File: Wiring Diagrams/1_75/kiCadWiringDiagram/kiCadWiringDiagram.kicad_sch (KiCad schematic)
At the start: 0 parts

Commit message: Designing schematic
Completed dual 12V inputs and converting them to 5V.

The rest of the circuit still remains.
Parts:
- added C1: C_Small, symbol Device:C_Small
- added C2, C3: C_Polarized_Small, symbol Device:C_Polarized_Small
- added D1, D2, D3: D_Schottky, symbol Device:D_Schottky
- added F1, F2: Fuse, symbol Device:Fuse
- added J1: ESP32, symbol Connector:Conn_01x10_Socket
- added J10: Boost Converter Input, symbol Connector:Conn_01x02_Socket
- added J11: Magnetometer MMC5603, symbol Connector:Conn_01x04_Socket
- added J12: Speaker Connector, symbol Connector:Conn_01x02_Socket
- added J2: Encoder Connector, symbol Connector:Conn_01x03_Socket
- added J3: LED Connector, symbol Connector:Conn_01x03_Socket
- added J4: Motor Connector, symbol Connector:Conn_01x03_Socket
- added J5: 12v Input 1, symbol Connector:Conn_01x02_Socket
- added J6: 12v Input 2, symbol Connector:Conn_01x02_Socket
- added J9: Boost Converter Output, symbol Connector:Conn_01x02_Socket
- added L1: L_Small, symbol Device:L_Small
- added U1: LM2596S-5, Package_TO_SOT_SMD:TO-263-5_TabPin3, symbol Regulator_Switching:LM2596S-5
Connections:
- new net: C3.1, L1.1, U1.4 (FB)
- new net: D3.2 (A), J5.1 (Pin_1), J6.1 (Pin_1), U1.3 (GND), U1.5 (~{ON}/OFF)
- new net: F1.2, J6.2 (Pin_2)
- new net: C1.1, C2.1, D1.1 (K), D2.1 (K)
- new net: D1.2 (A), F1.1
- new net: C1.2, C2.2, U1.1 (VIN)
- new net: D3.1 (K), L1.2, U1.2 (OUT)
- new net: D2.2 (A), F2.1
- new net: F2.2, J5.2 (Pin_2)

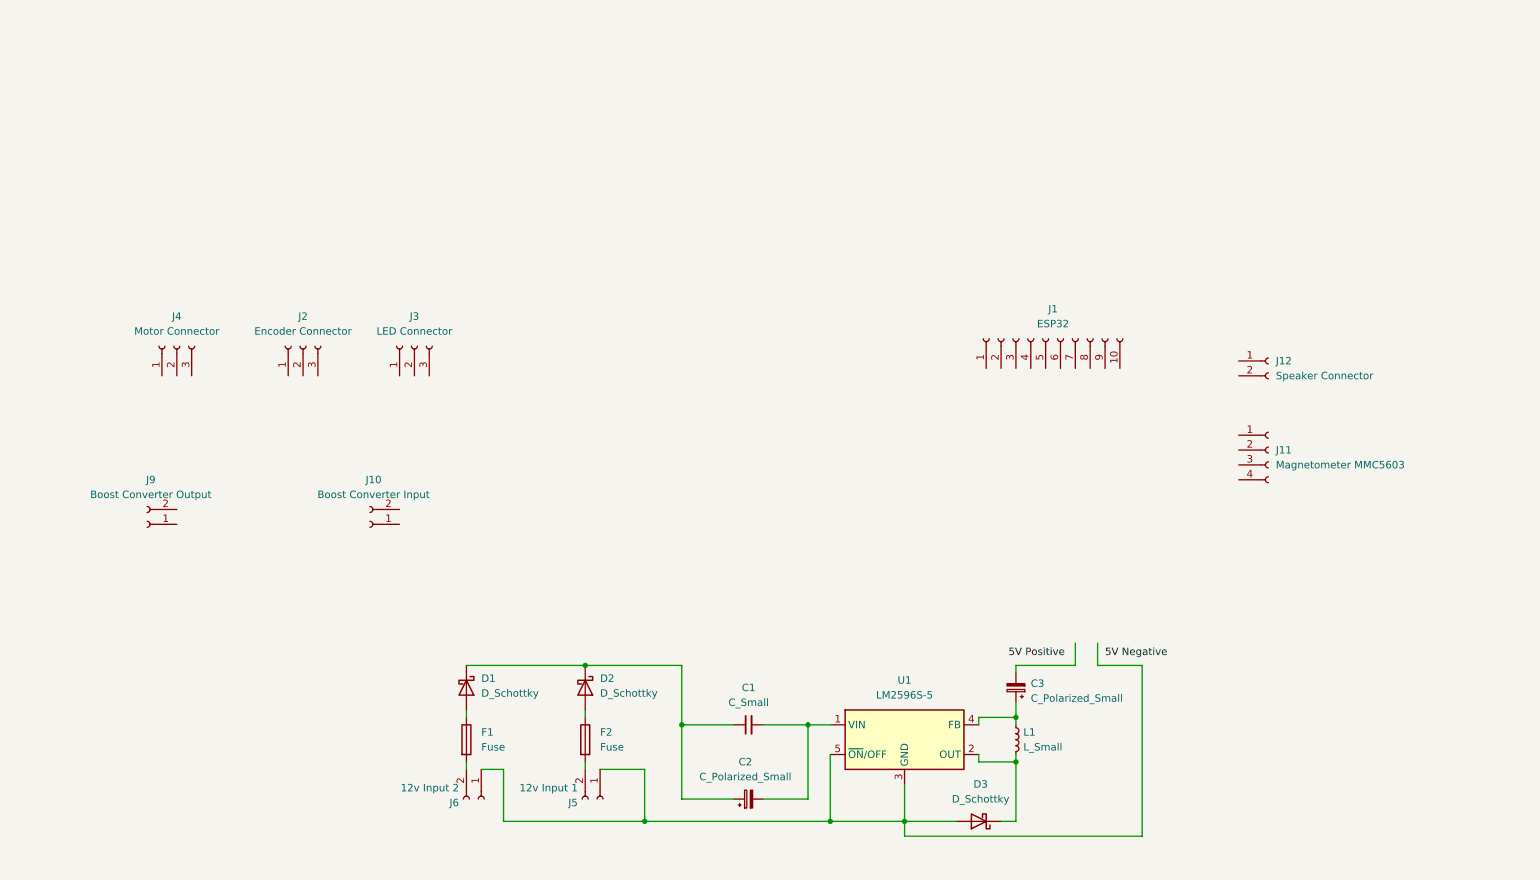
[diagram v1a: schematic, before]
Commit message: 5v to 10v conversion looks complete
fixed polarized capacitors
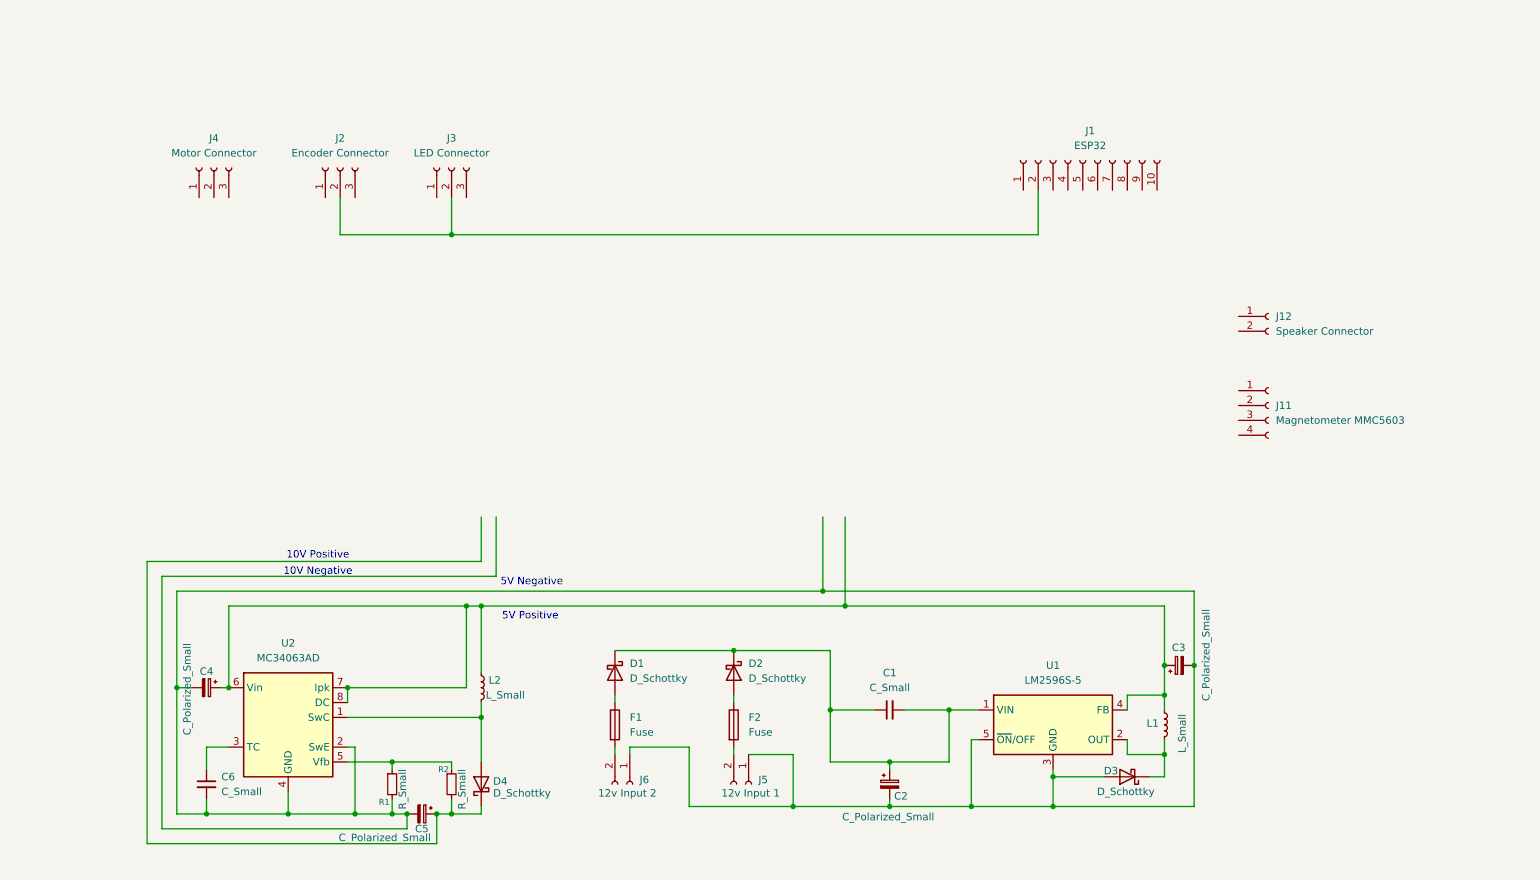
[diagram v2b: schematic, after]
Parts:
- removed J10: Boost Converter Input, symbol Connector:Conn_01x02_Socket
- removed J9: Boost Converter Output, symbol Connector:Conn_01x02_Socket
- added C4, C5: C_Polarized_Small, symbol Device:C_Polarized_Small
- added C6: C_Small, symbol Device:C_Small
- added D4: D_Schottky, symbol Device:D_Schottky
- added L2: L_Small, symbol Device:L_Small
- added R1, R2: R_Small, symbol Device:R_Small
- added U2: MC34063AD, Package_SO:SOIC-8_3.9x4.9mm_P1.27mm, symbol Regulator_Switching:MC34063AD
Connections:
- net at J1.2 (Pin_2): now also J2.2 (Pin_2), J3.2 (Pin_2)
- net at C3.1, L1.1, U1.4 (FB): now also C4.1, L2.1, U2.6 (Vin), U2.7 (Ipk), U2.8 (DC)
- net at C3.2: now also C2.2, D3.2 (A), J5.1 (Pin_1), J6.1 (Pin_1), U1.3 (GND), U1.5 (~{ON}/OFF), C4.2, C5.2, C6.2, R1.2, U2.2 (SwE), U2.4 (GND)
- net at C1.1, C2.1, D1.1 (K)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: now also C1.2, U1.1 (VIN)
- new net: D4.2 (A), L2.2, U2.1 (SwC)
- new net: C6.1, U2.3 (TC)
- new net: R1.1, R2.1, U2.5 (Vfb)
- new net: C5.1, D4.1 (K), R2.2
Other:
- note added: "10V Negative"
- note added: "10V Positive"
- note added: "5V Negative"
- note added: "5V Positive"
- moved on the sheet: C1, C2, C3, D1, D2, D3, F1, F2, J1, J11, J12, J2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

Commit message: Schematic done I think
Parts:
- removed J11: Magnetometer MMC5603, symbol Connector:Conn_01x04_Socket
- added U3: MMC5603NJ, MMC5603NJ:XDCR_MMC5603NJ, symbol MMC5603NJ:MMC5603NJ
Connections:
- net at J4.1 (Pin_1): now also C5.1, D4.1 (K), R2.2
- net at J4.2 (Pin_2): now also C2.2, C3.2, C4.2, C5.2, C6.2, D3.2 (A), J1.1 (Pin_1), J1.2 (Pin_2), J2.2 (Pin_2), J3.1 (Pin_1), J3.2 (Pin_2), J5.1 (Pin_1), J6.1 (Pin_1), R1.2, U1.3 (GND), U1.5 (~{ON}/OFF), U2.2 (SwE), U2.4 (GND), U3.A1 (VSA)
- net at J4.3 (Pin_3): now also J1.6 (Pin_6)
- net at J1.10 (Pin_10): now also J12.1 (Pin_1)
- net at J1.3 (Pin_3): now also J2.1 (Pin_1), U3.B1 (VDD)
- net at J1.4 (Pin_4): now also J3.3 (Pin_3)
- net at J1.5 (Pin_5): now also J2.3 (Pin_3)
- net at J1.7 (Pin_7): now also U3.B2 (SDA)
- net at J1.8 (Pin_8): now also U3.A2 (SCL)
- net at J1.9 (Pin_9): now also J12.2 (Pin_2)
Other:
- note added: "3V3"
- note added: "GND"
- note added: "SCL"
- note added: "SDA"
- note added: "SPKR+"
- note added: "SPKR-"
- moved on the sheet: J1, J12, J2, J3, J4

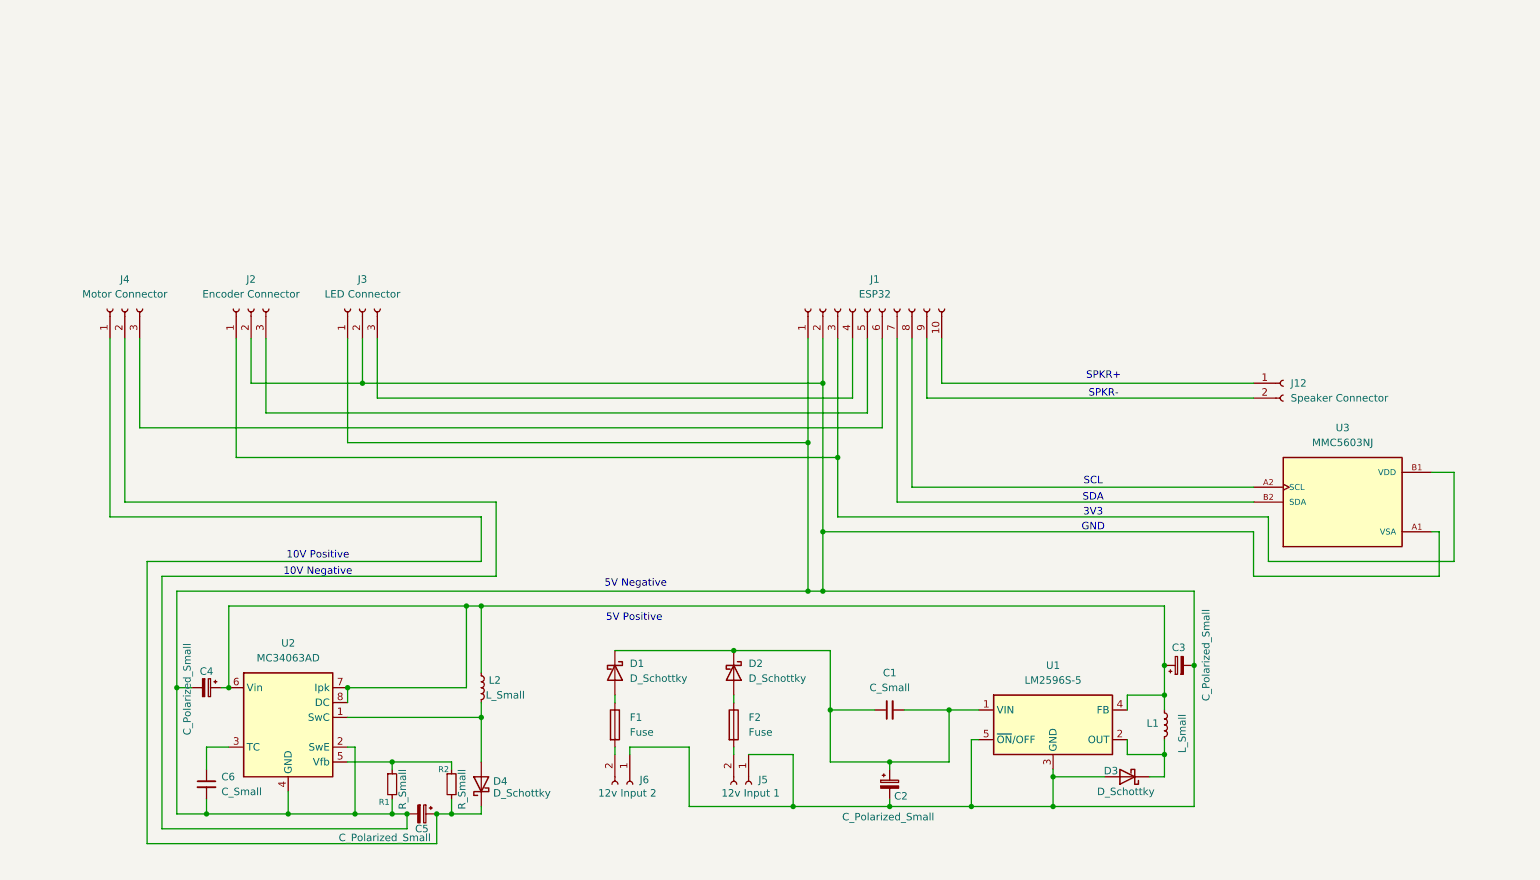
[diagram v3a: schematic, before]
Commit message: need to add motor driver ic
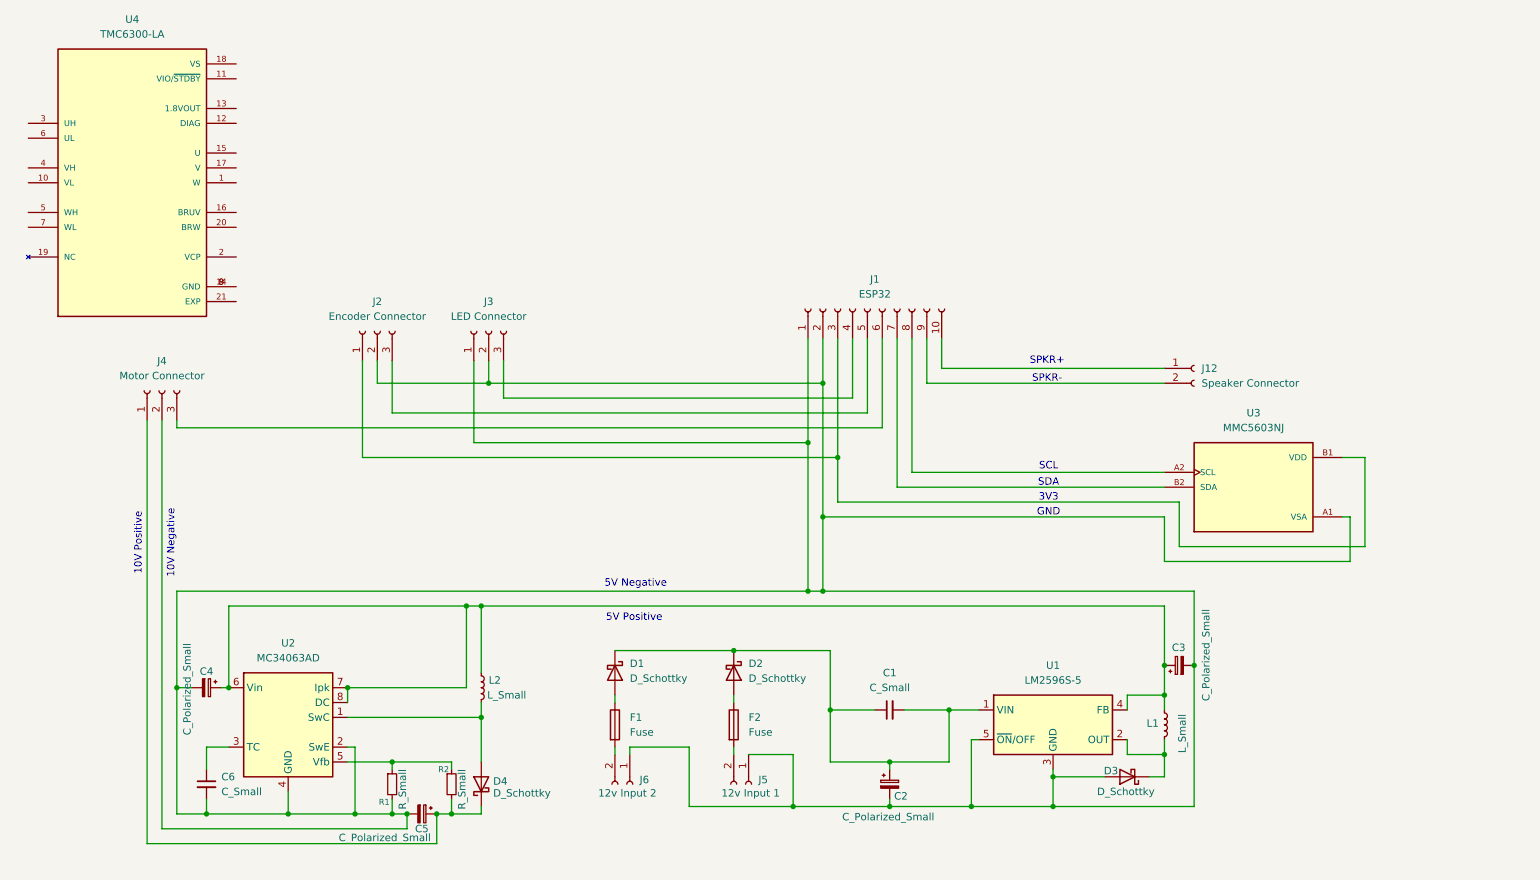
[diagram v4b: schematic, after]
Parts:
- added U4: TMC6300-LA, TMC6300-LA:QFN40P300X300X90-21N, symbol TMC6300-LA:TMC6300-LA
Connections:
- new net: U4.14 (GND), U4.8 (GND), U4.9 (GND)
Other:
- moved on the sheet: J12, J2, J3, J4, U3

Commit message: Needs IO expander as motor driver takes 6 GPIO pins
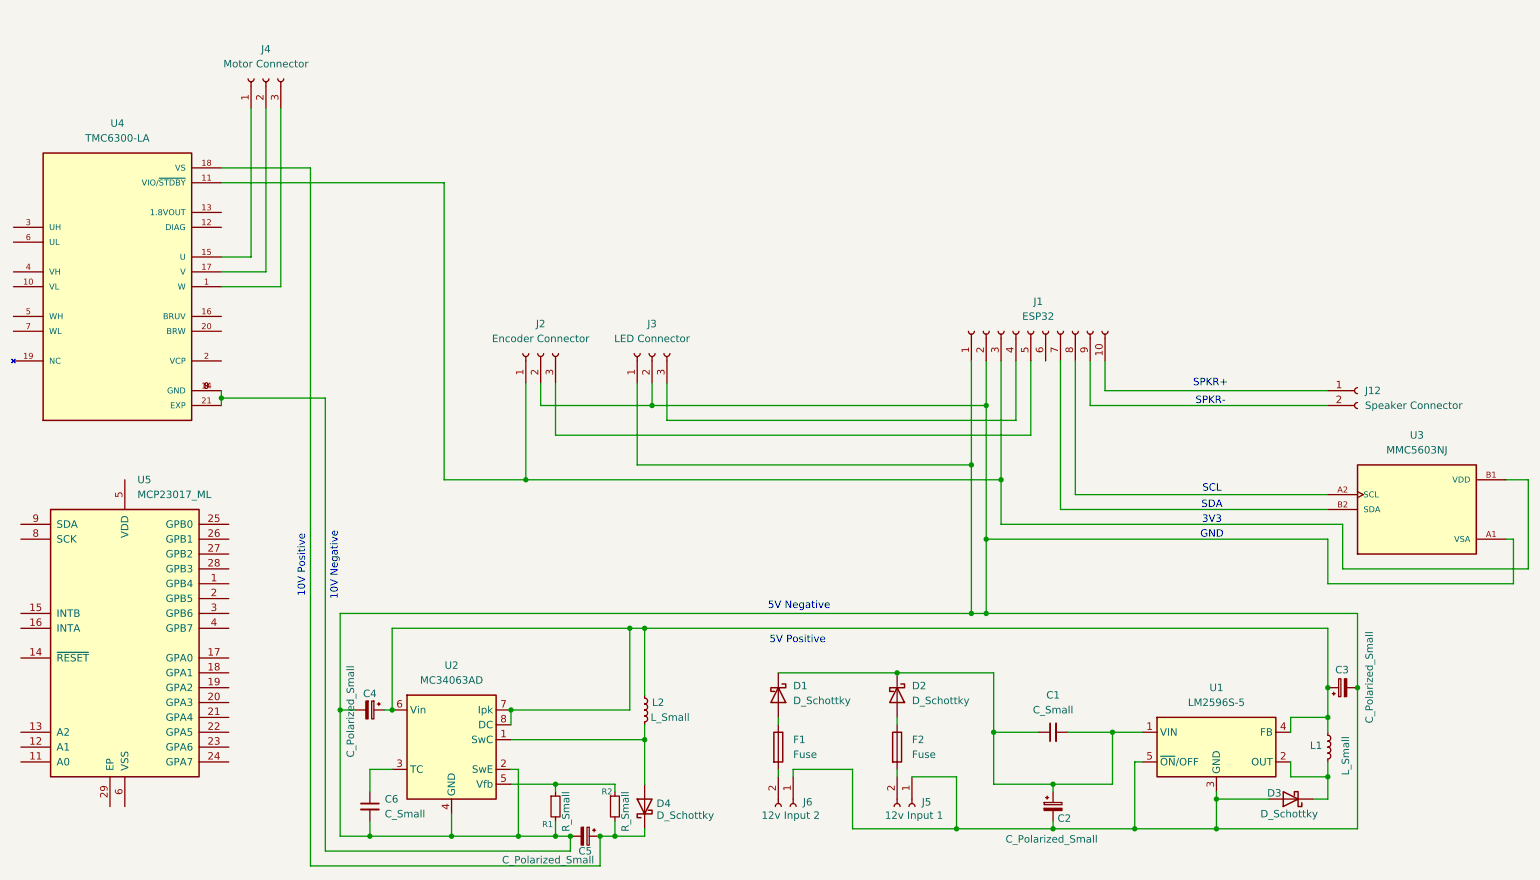
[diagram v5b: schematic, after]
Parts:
- added U5: MCP23017_ML, Package_DFN_QFN:QFN-28-1EP_6x6mm_P0.65mm_EP4.25x4.25mm, symbol Interface_Expansion:MCP23017_ML
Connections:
- net at C5.1, D4.1 (K), R2.2: now also U4.18 (VS); no longer J4.1 (Pin_1)
- net at C2.2, C3.2, C4.2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: now also U4.14 (GND), U4.21 (EXP), U4.8 (GND), U4.9 (GND); no longer J4.2 (Pin_2)
- net at J4.3 (Pin_3): now also U4.1 (W); no longer J1.6 (Pin_6)
- net at J1.3 (Pin_3), J2.1 (Pin_1), U3.B1 (VDD): now also U4.11 (VIO/~{STDBY})
- net at U4.15 (U): now also J4.1 (Pin_1)
- net at U4.17 (V): now also J4.2 (Pin_2)
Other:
- moved on the sheet: C1, C2, C3, C4, C5, C6, D1, D2, D3, D4, F1, F2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
